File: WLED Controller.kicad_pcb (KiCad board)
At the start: 2 copper layers, 100 x 100 mm, 77 parts, among them J1 Power, J2 LED1, J3 LED1, J4 LED1, J5 AudioJack4, J6 LED1, K1 SANYOU_SRD_Form_C, Q1 AOD403, Q2 BC548, U1 74AHCT125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

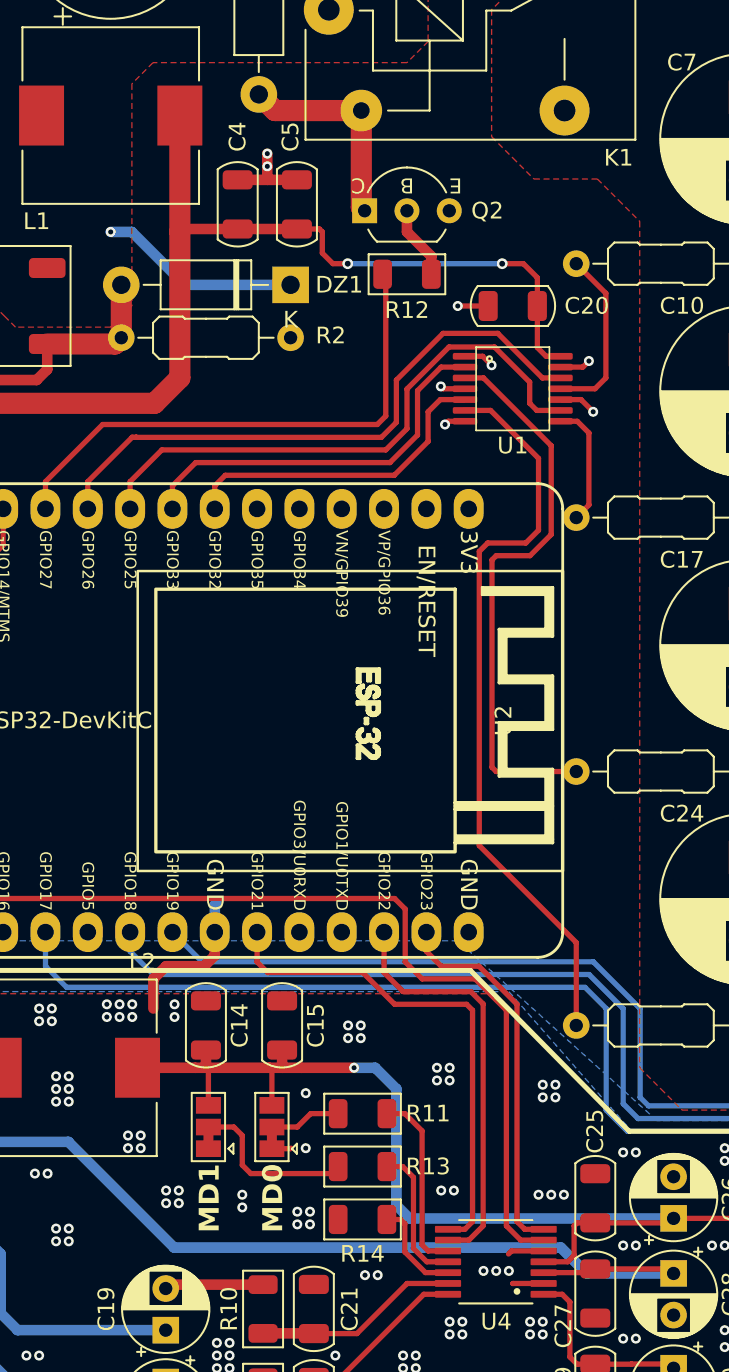
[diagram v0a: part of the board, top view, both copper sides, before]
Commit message: Switched relay driver to MOSFET. Optimizations.
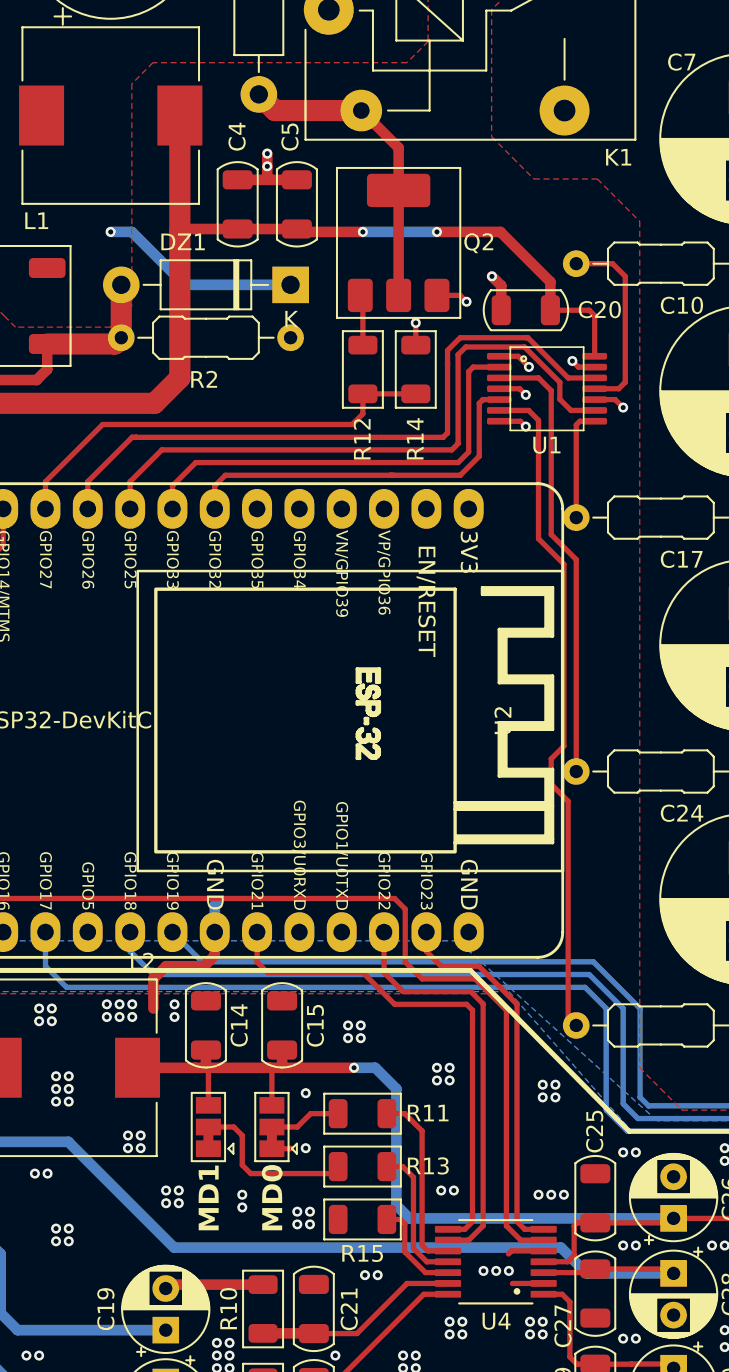
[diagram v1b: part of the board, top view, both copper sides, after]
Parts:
- added R14: 10k, PCM_Resistor_SMD_AKL:R_1206_3216Metric, F.Cu at (147.3, 82.5)
- Q2: value BC548 -> IRLL2705; footprint PCM_Package_TO_SOT_THT_AKL:TO-92_Inline_Wide_CBE -> PCM_Package_TO_SOT_SMD_AKL:SOT-223-3_TabPin2
- moved R12 6.30 mm to (144.1, 82.5), turned to -90 degrees
- moved Q2 2.81 mm to (146.3, 75.0), turned to 90 degrees
- moved U1 2.05 mm to (155.2, 83.7)
- moved C20 0.82 mm to (153.9, 79.0)
- renumbered R14 to R15
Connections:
- Q2 pad 1: Net-(D3-A) -> Net-(Q2-G)
- Q2 pad 2: Net-(Q2-B) -> Net-(D3-A)
- R12 pad 1: Net-(Q2-B) -> Net-(Q2-G)
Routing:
- net Net-(R4-Pad1): track 34.0 -> 26.9 mm
- net Net-(D3-A): track 12.6 -> 18.6 mm
- net RELAY_CTRL: track 32.3 -> 26.7 mm
- net Net-(R8-Pad1): track 45.0 -> 40.5 mm
- net Net-(Q2-B): track 4.42 -> 0.00 mm
- net GND: track 67.6 -> 71.5 mm, vias 194 -> 196
- net DATA2: track 34.5 -> 38.2 mm
- net DATA1: track 36.3 -> 39.7 mm
- net DATA3: track 23.5 -> 26.8 mm
- net DATA4: track 19.6 -> 22.7 mm
- net Net-(Q2-G): track 0.00 -> 3.05 mm
- net +5V_D: track 190.4 -> 191.7 mm
- net Net-(R1-Pad1): track 10.7 -> 11.6 mm
- net Net-(R3-Pad1): track 7.49 -> 6.76 mm

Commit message: Optimizations
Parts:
- added JP1: R2 GND, Jumper:SolderJumper-3_P1.3mm_Bridged12_Pad1.0x1.5mm, F.Cu at (123.7, 137.7)
- moved C8 11.2 mm to (123.0, 84.1), turned to 180 degrees
- moved D2 3.99 mm to (106.9, 84.6)
- moved D1 3.83 mm to (106.8, 76.7)
- moved R6 3.22 mm to (112.4, 82.0)
- moved R5 3.20 mm to (112.4, 76.5)
- renumbered C21 to C20, C22 to C21, C20 to C22, JP1 to JP2, JP2 to JP3
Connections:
- J5 pad R2: GND -> Net-(JP1-C)
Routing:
- net Net-(JP1-C): track 0.00 -> 28.3 mm
- net Net-(DZ1-A): track 24.2 -> 11.1 mm
- net Net-(U2-MTCK/GPIO13/ADC2_CH4): track 21.2 -> 22.7 mm
- net Net-(U2-MTMS/GPIO14/ADC2_CH6): track 25.9 -> 27.2 mm
- net GND: track 71.5 -> 70.2 mm, vias 196 -> 233
- net Net-(D2-A): track 6.85 -> 6.07 mm
- net Net-(D1-A): track 6.69 -> 5.93 mm
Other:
- board text added: "38-Pin"
- board text added: "Audio in"
- board text added: "POWER"
- board text added: "R2->GND"
- board text removed: "Audio In"
- board text removed: "PWR"

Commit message: Optimizations
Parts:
- moved R5 1.14 mm to (111.3, 76.5)
- moved R6 1.14 mm to (111.3, 82.0)
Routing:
- net Net-(Q1-D): track 6.74 -> 0.00 mm
- net Net-(J6-Pin_1): track 6.16 -> 0.00 mm
- net Net-(J4-Pin_1): track 6.16 -> 0.00 mm
- net Net-(J3-Pin_1): track 6.16 -> 0.00 mm
- net Net-(J2-Pin_1): track 6.16 -> 0.00 mm
- net Net-(D2-A): track 6.07 -> 4.92 mm
- net Net-(D1-A): track 5.93 -> 4.79 mm
- added copper zone on F.Cu, net Net-(J2-Pin_1)
- added copper zone on F.Cu, net Net-(J3-Pin_1)
- added copper zone on F.Cu, net Net-(J4-Pin_1)
- added copper zone on F.Cu, net Net-(J6-Pin_1)
- added copper zone on F.Cu, net Net-(Q1-D)
